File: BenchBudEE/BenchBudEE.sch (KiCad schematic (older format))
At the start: 0 parts

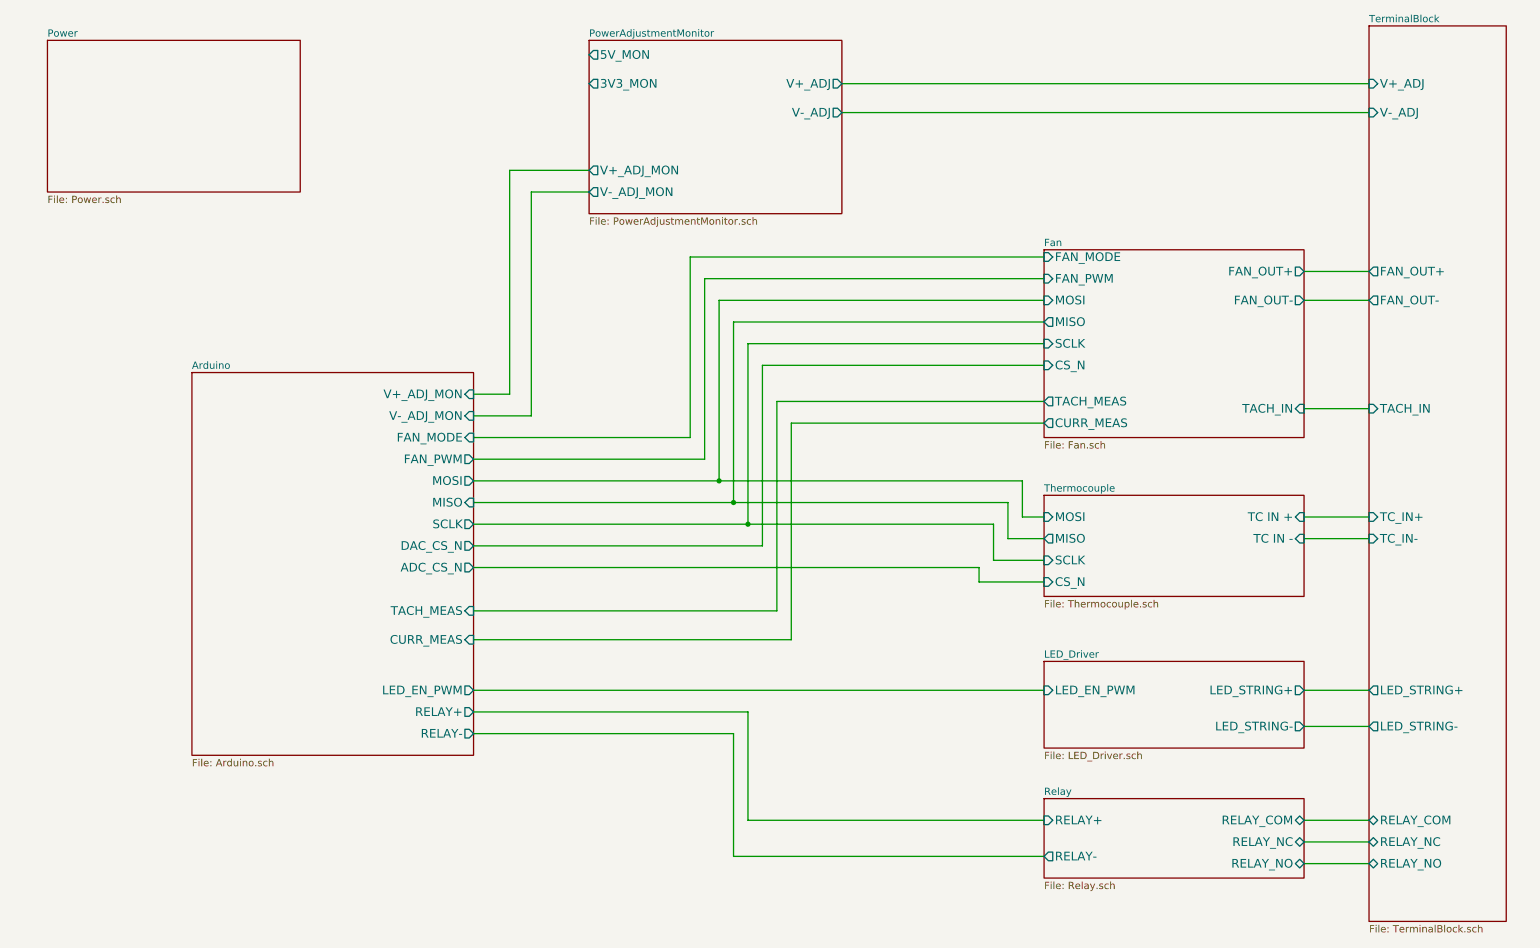
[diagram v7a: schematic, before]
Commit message: Associated the Thermocouple components.
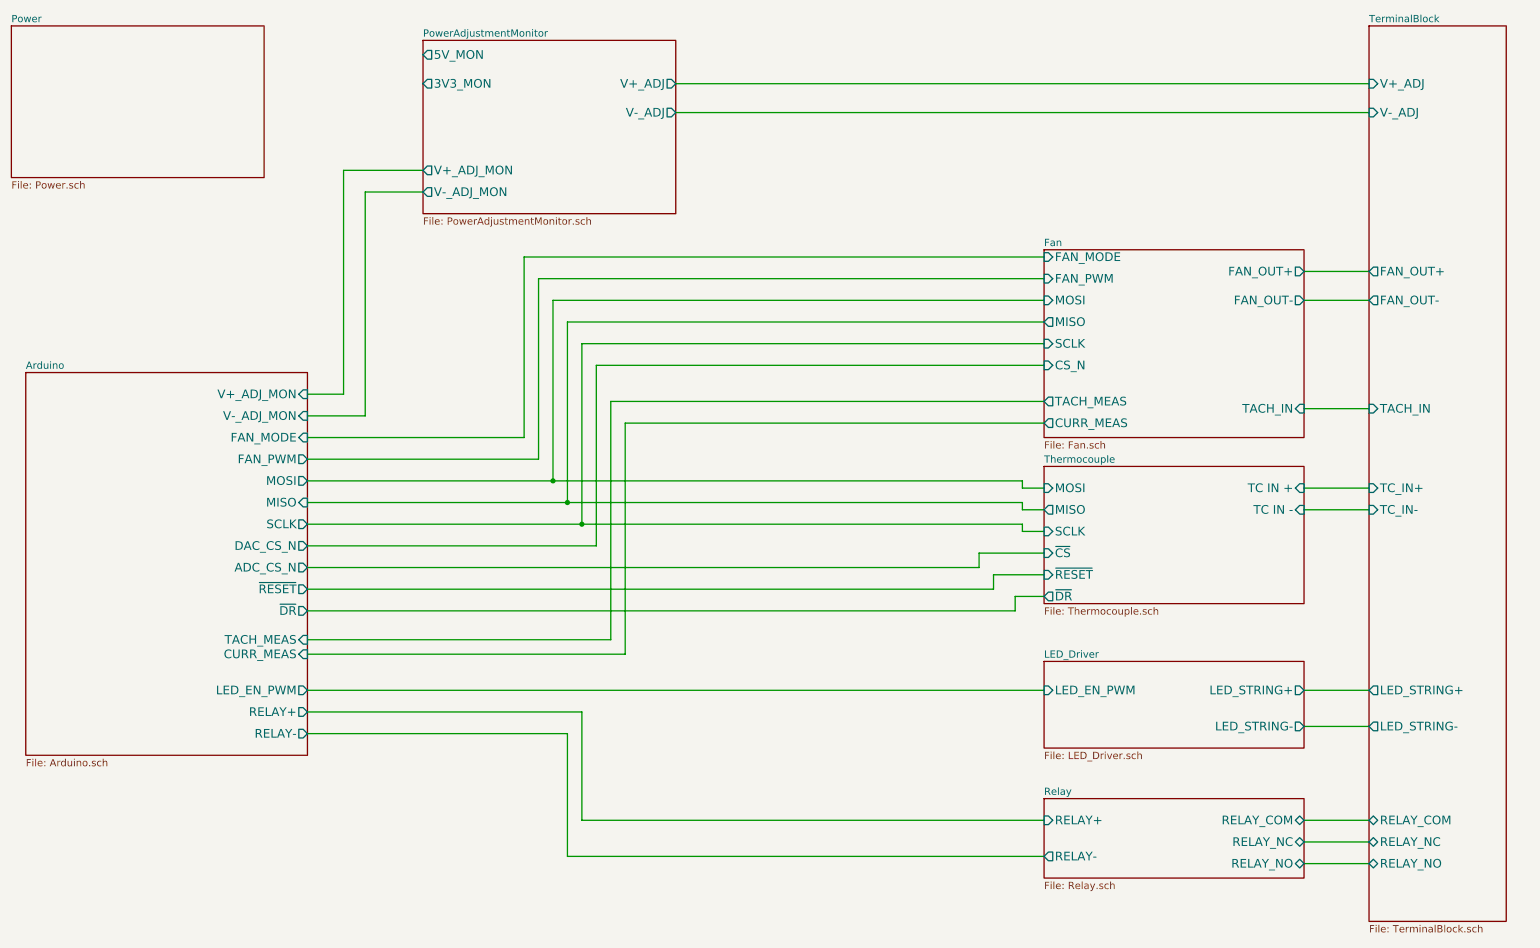
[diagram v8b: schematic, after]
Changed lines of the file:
@@
 Sheet 1 9
 Title ""
-Date "20 feb 2014"
+Date "21 feb 2014"
 Rev ""
 Comp ""
@@
 $EndDescr
 $Sheet
-S 7850 4000 1800 700
+S 7850 3800 1800 950
 U 52EC4DA4
 F0 "Thermocouple" 50
 F1 "Thermocouple.sch" 50
-F2 "TC IN +" I R 9650 4150 60
-F3 "TC IN -" I R 9650 4300 60
-F4 "MOSI" I L 7850 4150 60
-F5 "MISO" O L 7850 4300 60
-F6 "SCLK" I L 7850 4450 60
-F7 "CS_N" I L 7850 4600 60
+F2 "TC IN +" I R 9650 3950 60
+F3 "TC IN -" I R 9650 4100 60
+F4 "MOSI" I L 7850 3950 60
+F5 "MISO" O L 7850 4100 60
+F6 "SCLK" I L 7850 4250 60
+F7 "~CS" I L 7850 4400 60
+F8 "~RESET" I L 7850 4550 60
+F9 "~DR" O L 7850 4700 60
 $EndSheet
 $Sheet
@@
 $EndSheet
 $Sheet
-S 950  850  1750 1050
+S 700  750  1750 1050
 U 52EC4DDC
 F0 "Power" 50
@@
 $EndSheet
 $Sheet
-S 4700 850  1750 1200
+S 3550 850  1750 1200
 U 52F627C8
 F0 "PowerAdjustmentMonitor" 50
 F1 "PowerAdjustmentMonitor.sch" 50
-F2 "V+_ADJ" O R 6450 1150 60
-F3 "V-_ADJ" O R 6450 1350 60
-F4 "3V3_MON" O L 4700 1150 60
-F5 "5V_MON" O L 4700 950 60
-F6 "V+_ADJ_MON" O L 4700 1750 60
-F7 "V-_ADJ_MON" O L 4700 1900 60
+F2 "V+_ADJ" O R 5300 1150 60
+F3 "V-_ADJ" O R 5300 1350 60
+F4 "3V3_MON" O L 3550 1150 60
+F5 "5V_MON" O L 3550 950 60
+F6 "V+_ADJ_MON" O L 3550 1750 60
+F7 "V-_ADJ_MON" O L 3550 1900 60
 $EndSheet
 $Sheet
@@
 $EndSheet
 Wire Wire Line
-	10100 1150 6450 1150
-Wire Wire Line
-	10100 1350 6450 1350
+	10100 1150 5300 1150
+Wire Wire Line
+	10100 1350 5300 1350
 $Sheet
 S 10100 750  950  6200
@@
 F7 "LED_STRING+" O L 10100 5350 60
 F8 "LED_STRING-" O L 10100 5600 60
-F9 "TC_IN+" I L 10100 4150 60
-F10 "TC_IN-" I L 10100 4300 60
+F9 "TC_IN+" I L 10100 3950 60
+F10 "TC_IN-" I L 10100 4100 60
 F11 "RELAY_COM" B L 10100 6250 60
 F12 "RELAY_NO" B L 10100 6550 60
@@
 	9650 6250 10100 6250
 Wire Wire Line
-	3900 3300 4150 3300
-Wire Wire Line
-	4150 3300 4150 1750
-Wire Wire Line
-	4150 1750 4700 1750
-Wire Wire Line
-	3900 3450 4300 3450
-Wire Wire Line
-	4300 3450 4300 1900
-Wire Wire Line
-	4300 1900 4700 1900
-$Sheet
-S 1950 3150 1950 2650
+	2750 3300 3000 3300
+Wire Wire Line
+	3000 3300 3000 1750
+Wire Wire Line
+	3000 1750 3550 1750
+Wire Wire Line
+	2750 3450 3150 3450
+Wire Wire Line
+	3150 3450 3150 1900
+Wire Wire Line
+	3150 1900 3550 1900
+$Sheet
+S 800  3150 1950 2650
 U 52EC4D59
 F0 "Arduino" 50
 F1 "Arduino.sch" 50
-F2 "MOSI" O R 3900 3900 60
-F3 "MISO" I R 3900 4050 60
-F4 "SCLK" O R 3900 4200 60
-F5 "TACH_MEAS" I R 3900 4800 60
-F6 "RELAY+" O R 3900 5500 60
-F7 "RELAY-" O R 3900 5650 60
-F8 "CURR_MEAS" I R 3900 5000 60
-F9 "V+_ADJ_MON" I R 3900 3300 60
-F10 "V-_ADJ_MON" I R 3900 3450 60
-F11 "LED_EN_PWM" O R 3900 5350 60
-F12 "DAC_CS_N" O R 3900 4350 60
-F13 "ADC_CS_N" O R 3900 4500 60
-F14 "FAN_PWM" O R 3900 3750 60
-F15 "FAN_MODE" I R 3900 3600 60
-$EndSheet
-Wire Wire Line
-	3900 3750 5500 3750
-Wire Wire Line
-	3900 3900 7700 3900
-Wire Wire Line
-	5600 3900 5600 2650
-Wire Wire Line
-	5600 2650 7850 2650
-Wire Wire Line
-	3900 4050 7600 4050
-Wire Wire Line
-	5700 4050 5700 2800
-Wire Wire Line
-	5700 2800 7850 2800
-Wire Wire Line
-	6000 3350 6000 4800
-Wire Wire Line
-	6000 3350 7850 3350
-Wire Wire Line
-	6100 3500 6100 5000
-Wire Wire Line
-	6100 3500 7850 3500
-Wire Wire Line
-	9650 4150 10100 4150
-Wire Wire Line
-	9650 4300 10100 4300
+F2 "MOSI" O R 2750 3900 60
+F3 "MISO" I R 2750 4050 60
+F4 "SCLK" O R 2750 4200 60
+F5 "TACH_MEAS" I R 2750 5000 60
+F6 "RELAY+" O R 2750 5500 60
+F7 "RELAY-" O R 2750 5650 60
+F8 "CURR_MEAS" I R 2750 5100 60
+F9 "V+_ADJ_MON" I R 2750 3300 60
+F10 "V-_ADJ_MON" I R 2750 3450 60
+F11 "LED_EN_PWM" O R 2750 5350 60
+F12 "DAC_CS_N" O R 2750 4350 60
+F13 "ADC_CS_N" O R 2750 4500 60
+F14 "FAN_PWM" O R 2750 3750 60
+F15 "FAN_MODE" I R 2750 3600 60
+F16 "~RESET" O R 2750 4650 60
+F17 "~DR" O R 2750 4800 60
+$EndSheet
+Wire Wire Line
+	2750 3750 4350 3750
+Wire Wire Line
+	2750 3900 7700 3900
+Wire Wire Line
+	4450 3900 4450 2650
+Wire Wire Line
+	4450 2650 7850 2650
+Wire Wire Line
+	2750 4050 7700 4050
+Wire Wire Line
+	4550 4050 4550 2800
+Wire Wire Line
+	4550 2800 7850 2800
+Wire Wire Line
+	4850 3350 4850 5000
+Wire Wire Line
+	4850 3350 7850 3350
+Wire Wire Line
+	4950 3500 4950 5100
+Wire Wire Line
+	4950 3500 7850 3500
+Wire Wire Line
+	9650 3950 10100 3950
+Wire Wire Line
+	9650 4100 10100 4100
 Wire Wire Line
 	9650 5350 10100 5350
@@
 	9650 5600 10100 5600
 Wire Wire Line
-	6100 5000 3900 5000
-Wire Wire Line
-	6000 4800 3900 4800
-Wire Wire Line
-	7850 2950 5800 2950
-Wire Wire Line
-	5800 2950 5800 4200
-Wire Wire Line
-	3900 4200 7500 4200
-Wire Wire Line
-	3900 4350 5900 4350
-Wire Wire Line
-	5900 4350 5900 3100
-Wire Wire Line
-	5900 3100 7850 3100
-Wire Wire Line
-	7850 4150 7700 4150
-Wire Wire Line
-	7700 4150 7700 3900
-Connection ~ 5600 3900
-Wire Wire Line
-	7850 4300 7600 4300
-Wire Wire Line
-	7600 4300 7600 4050
-Connection ~ 5700 4050
-Wire Wire Line
-	7850 4450 7500 4450
-Wire Wire Line
-	7500 4450 7500 4200
-Connection ~ 5800 4200
-Wire Wire Line
-	7850 4600 7400 4600
-Wire Wire Line
-	7400 4600 7400 4500
-Wire Wire Line
-	7400 4500 3900 4500
-Wire Wire Line
-	3900 5350 7850 5350
-Wire Wire Line
-	3900 5650 5700 5650
-Wire Wire Line
-	5700 5650 5700 6500
-Wire Wire Line
-	5700 6500 7850 6500
-Wire Wire Line
-	3900 5500 5800 5500
-Wire Wire Line
-	5800 5500 5800 6250
-Wire Wire Line
-	5800 6250 7850 6250
+	7850 2950 4650 2950
+Wire Wire Line
+	4650 2950 4650 4200
+Wire Wire Line
+	2750 4200 7700 4200
+Wire Wire Line
+	2750 4350 4750 4350
+Wire Wire Line
+	4750 4350 4750 3100
+Wire Wire Line
+	4750 3100 7850 3100
+Connection ~ 4450 3900
+Connection ~ 4550 4050
+Connection ~ 4650 4200
+Wire Wire Line
+	7400 4500 2750 4500
+Wire Wire Line
+	2750 5350 7850 5350
+Wire Wire Line
+	2750 5650 4550 5650
+Wire Wire Line
+	4550 5650 4550 6500
+Wire Wire Line
+	4550 6500 7850 6500
+Wire Wire Line
+	2750 5500 4650 5500
+Wire Wire Line
+	4650 5500 4650 6250
+Wire Wire Line
+	4650 6250 7850 6250
 Wire Wire Line
 	9650 6400 10100 6400
@@
 	9650 6550 10100 6550
 Wire Wire Line
-	5500 3750 5500 2500
-Wire Wire Line
-	5500 2500 7850 2500
-Wire Wire Line
-	7850 2350 5400 2350
-Wire Wire Line
-	5400 2350 5400 3600
-Wire Wire Line
-	5400 3600 3900 3600
+	4350 3750 4350 2500
+Wire Wire Line
+	4350 2500 7850 2500
+Wire Wire Line
+	7850 2350 4250 2350
+Wire Wire Line
+	4250 2350 4250 3600
+Wire Wire Line
+	4250 3600 2750 3600
+Wire Wire Line
+	7700 3900 7700 3950
+Wire Wire Line
+	7700 3950 7850 3950
+Wire Wire Line
+	7700 4050 7700 4100
+Wire Wire Line
+	7700 4100 7850 4100
+Wire Wire Line
+	7700 4200 7700 4250
+Wire Wire Line
+	7700 4250 7850 4250
+Wire Wire Line
+	7400 4500 7400 4400
+Wire Wire Line
+	7400 4400 7850 4400
+Wire Wire Line
+	4950 5100 2750 5100
+Wire Wire Line
+	4850 5000 2750 5000
+Wire Wire Line
+	2750 4650 7500 4650
+Wire Wire Line
+	7500 4650 7500 4550
+Wire Wire Line
+	7500 4550 7850 4550
+Wire Wire Line
+	2750 4800 7650 4800
+Wire Wire Line
+	7650 4800 7650 4700
+Wire Wire Line
+	7650 4700 7850 4700
 $EndSCHEMATC
